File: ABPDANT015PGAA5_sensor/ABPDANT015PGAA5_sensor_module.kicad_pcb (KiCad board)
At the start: 4 copper layers, 29 x 29.5 mm, 9 parts, among them J1 Conn_02x04_Odd_Even, J2 Conn_02x07_Odd_Even, U1 ABPDANT060MGAA5, U2 LM358

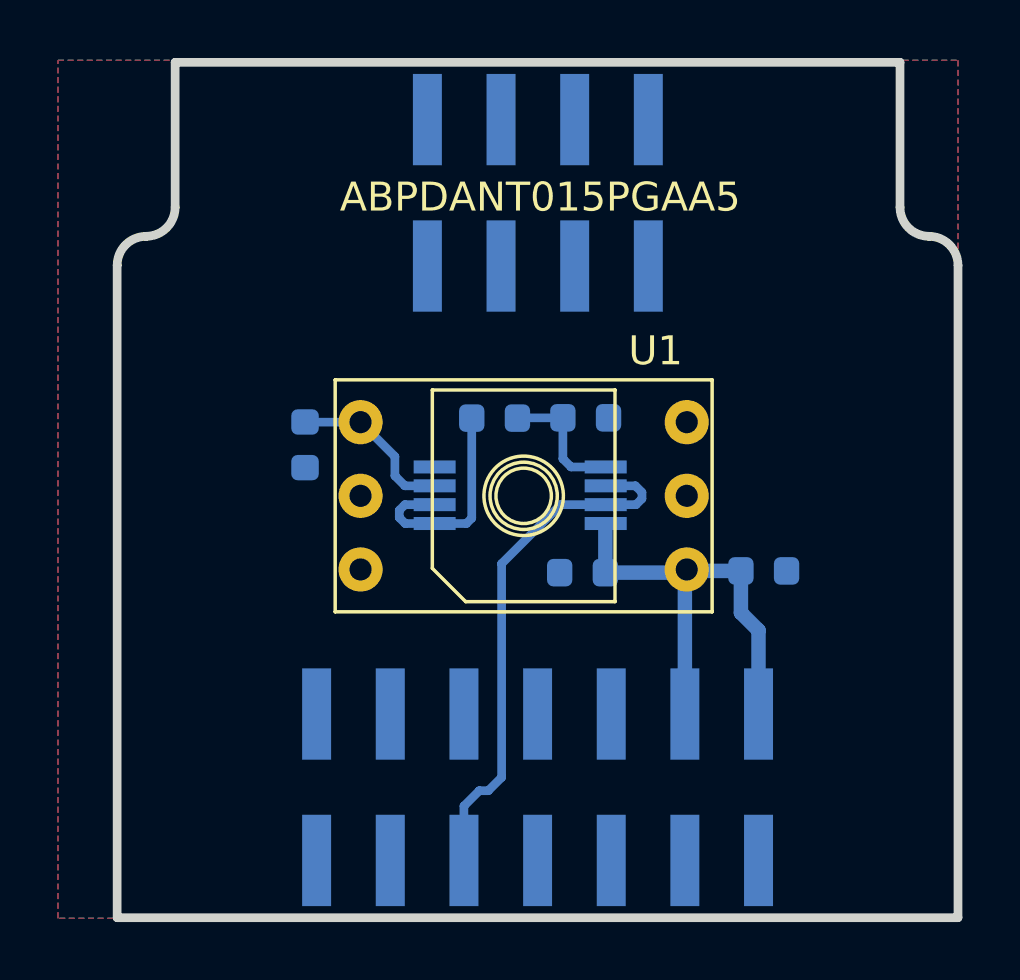
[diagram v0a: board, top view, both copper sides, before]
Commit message: Position for J2 U1 and U2 modified
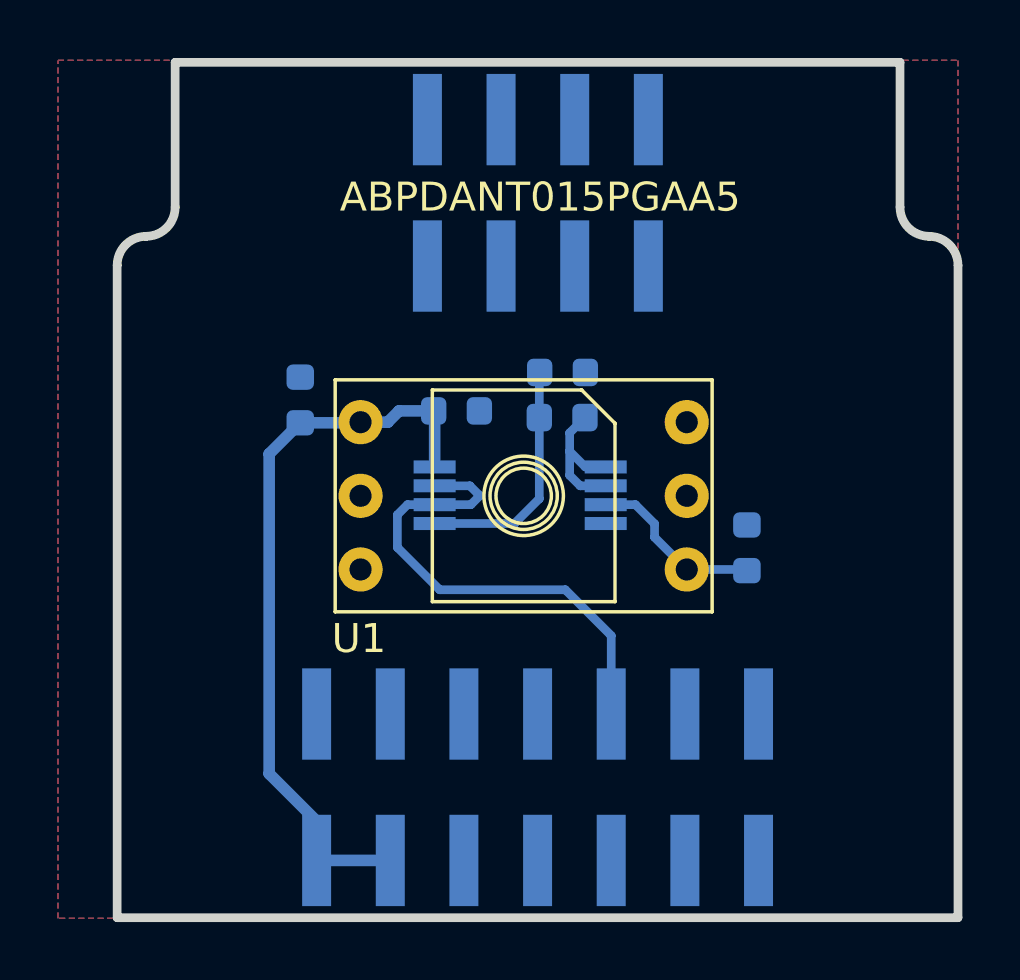
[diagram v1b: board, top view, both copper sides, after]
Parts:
- moved C1 17.0 mm to (104.8, 41.7), turned to 90 degrees
- moved C2 15.6 mm to (120.2, 46.8), turned to 90 degrees
- moved C3 7.07 mm to (110.2, 42.1), turned to 0 degrees
- moved R1 2.33 mm to (113.8, 42.3), turned to 0 degrees
- moved R2 1.76 mm to (113.8, 40.8)
- turned J2 to 270 degrees
- turned U1 to 270 degrees
- turned U2 to 180 degrees
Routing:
- net +5V: track 21.2 -> 25.5 mm
- net Net-(R1-Pad1): track 4.58 -> 8.32 mm
- net Net-(R1-Pad2): track 7.66 -> 5.07 mm
- net /SPI_CS: track 1.20 -> 0.00 mm

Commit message: Modified sensor modules and created module for 403-SFM3020 sensor
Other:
- rule pad_to_mask_clearance: 0.2 -> 0
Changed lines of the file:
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@@
-(kicad_pcb (version 20171130) (host pcbnew 5.1.10-88a1d61d58~90~ubuntu20.04.1)
+(kicad_pcb (version 20171130) (host pcbnew 5.1.12-84ad8e8a86~92~ubuntu20.04.1)
   (general
     (thickness 1.6)
@@
   )
   (setup
-    (last_trace_width 0.3)
+    (last_trace_width 0.2)
     (user_trace_width 0.2)
     (user_trace_width 0.3)
@@
     (pad_size 0.6 1.65)
     (pad_drill 0)
-    (pad_to_mask_clearance 0.2)
-    (solder_mask_min_width 0.2)
+    (pad_to_mask_clearance 0)
     (aux_axis_origin 0 0)
     (visible_elements FFFFFF7F)
     (pcbplotparams
-      (layerselection 0x010fc_ffffffff)
+      (layerselection 0x010fc_fffffff9)
       (usegerberextensions false)
       (usegerberattributes false)
@@
     (pad 6 thru_hole circle (at -2.54 5.625 270) (size 1.524 1.524) (drill 0.762) (layers *.Cu *.Mask)
       (net 3 +5V))
+    (model ${KIPRJMOD}/../kicad-modules/shapes3d/abpdant005pgaa5.stp
+      (offset (xyz -40 -27.58 5))
+      (scale (xyz 1 1 1))
+      (rotate (xyz 0 0 -90))
+    )
   )
   (module Capacitor_SMD:C_0603_1608Metric (layer B.Cu)
